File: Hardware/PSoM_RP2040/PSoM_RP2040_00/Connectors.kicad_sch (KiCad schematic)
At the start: 8 parts, among them J201 Bare PCB USB C, J202 DF40C-60DP-0.4V(51)

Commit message: updated bas de page
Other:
- title: PSoM - ESP S3 -> PSoM - RP2040
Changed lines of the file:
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@@
   (paper "A4")
   (title_block
-    (title "PSoM - ESP S3")
-    (date "2023-04-17")
+    (title "PSoM - RP2040")
+    (date "2024-02-28")
     (rev "HW00")
     (company "PumaCorp")

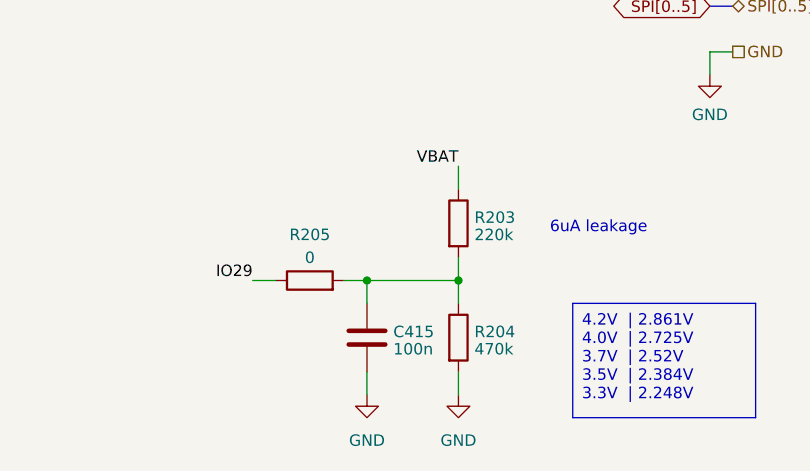
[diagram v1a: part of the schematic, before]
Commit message: small adjustements on rp2040 routing
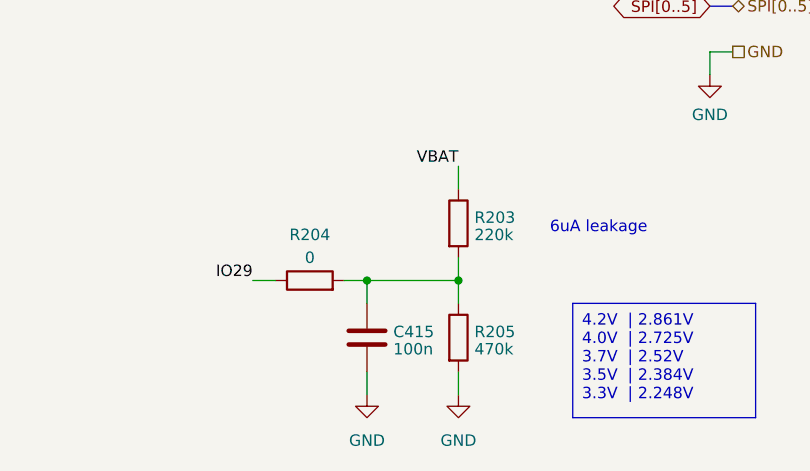
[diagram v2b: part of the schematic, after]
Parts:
- renumbered R205 to R204, R204 to R205
